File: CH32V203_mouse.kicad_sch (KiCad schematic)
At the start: 30 parts, among them J1 USB_C_Receptacle_USB2.0_16P_u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, J2 Conn_01x05_Pin, J3 Conn_01x04_Pin, SW1 SW_Push, U1 CH32V203G6U6, U2 USBLC6-2SC6, U3 XC6206P332MR, X1 16MHz

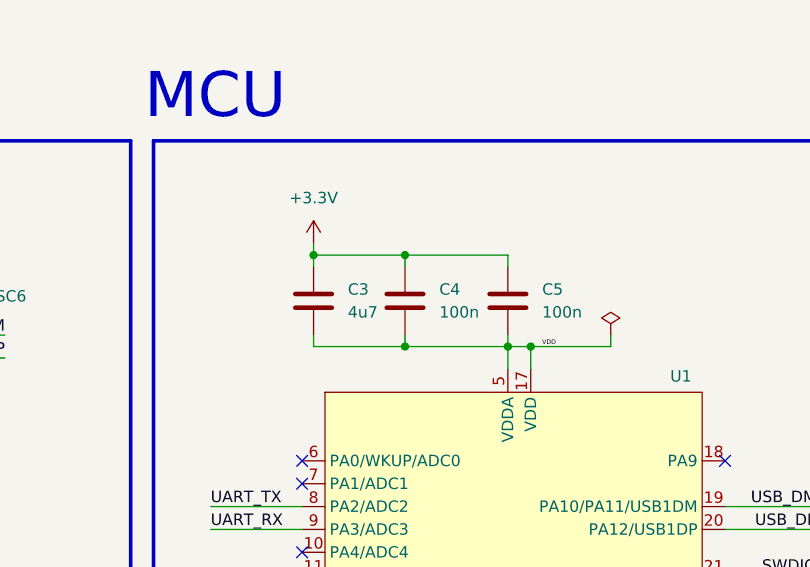
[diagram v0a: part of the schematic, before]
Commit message: Better PCB layout decoupling capacitors fixed changed LEDs footprints to correct ones
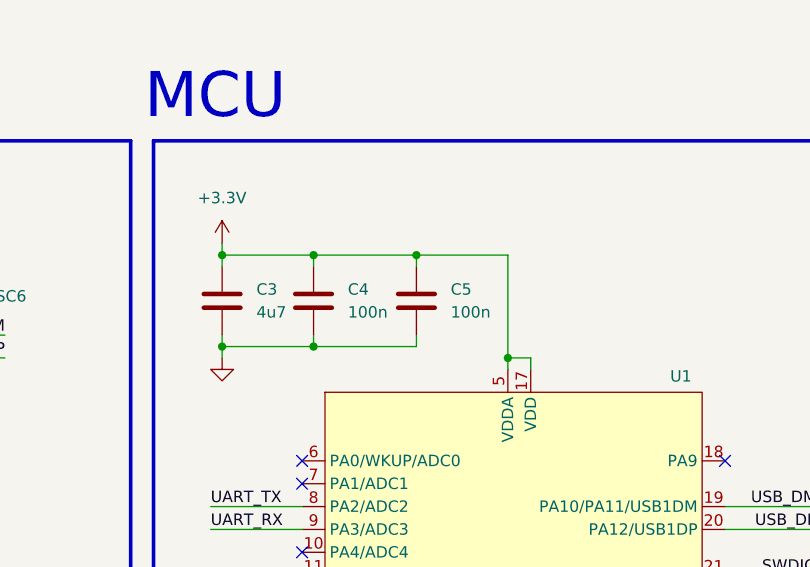
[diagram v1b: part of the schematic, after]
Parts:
- D1: footprint Capacitor_SMD:C_0402_1005Metric -> LED_SMD:LED_0603_1608Metric
- D2: footprint Capacitor_SMD:C_0402_1005Metric -> Diode_SMD:D_0603_1608Metric
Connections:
- net +3.3V: now also U1.17 (VDD), U1.5 (VDDA)
- net GND: now also C3.2, C4.2, C5.2
- removed net VDD: C3.2, C4.2, C5.2, U1.17 (VDD), U1.5 (VDDA)
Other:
- moved on the sheet: C3, C4, C5

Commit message: Changed stack up to a 4-layer board
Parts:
- D2: footprint Diode_SMD:D_0603_1608Metric -> LED_SMD:LED_0603_1608Metric
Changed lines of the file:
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@@
 			)
 		)
-		(property "Footprint" "Diode_SMD:D_0603_1608Metric"
+		(property "Footprint" "LED_SMD:LED_0603_1608Metric"
 			(at 259.08 52.07 0)
 			(effects

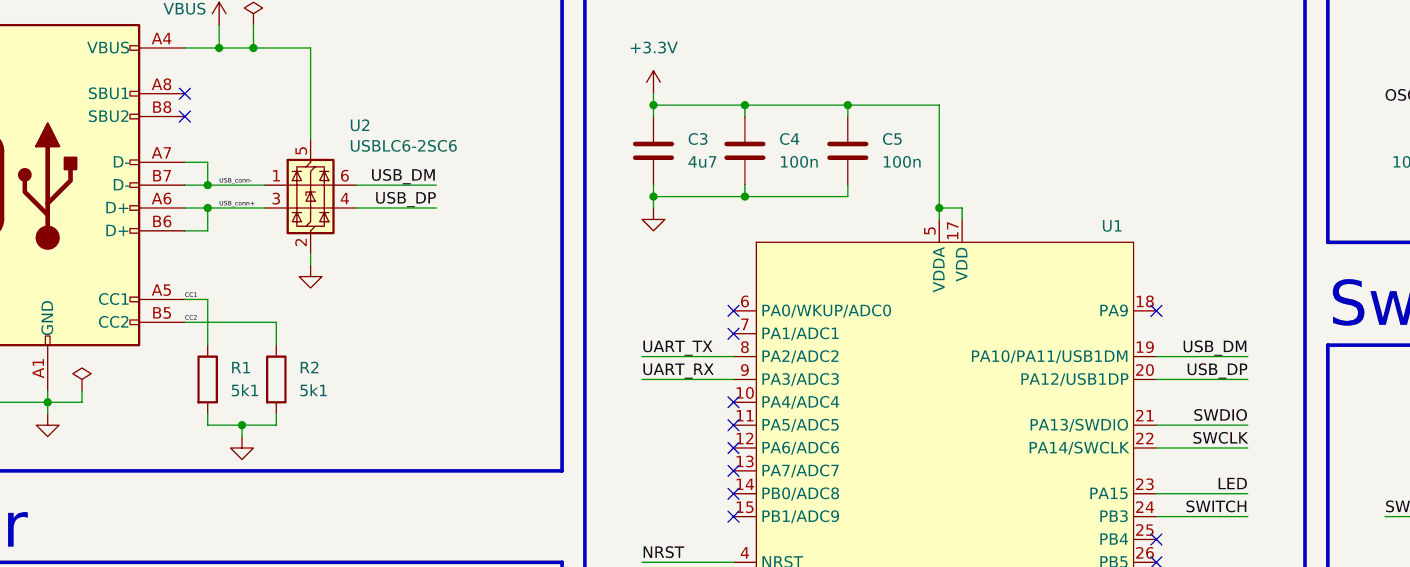
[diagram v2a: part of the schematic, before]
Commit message: Signals routed Constraints updated USB labels fixed
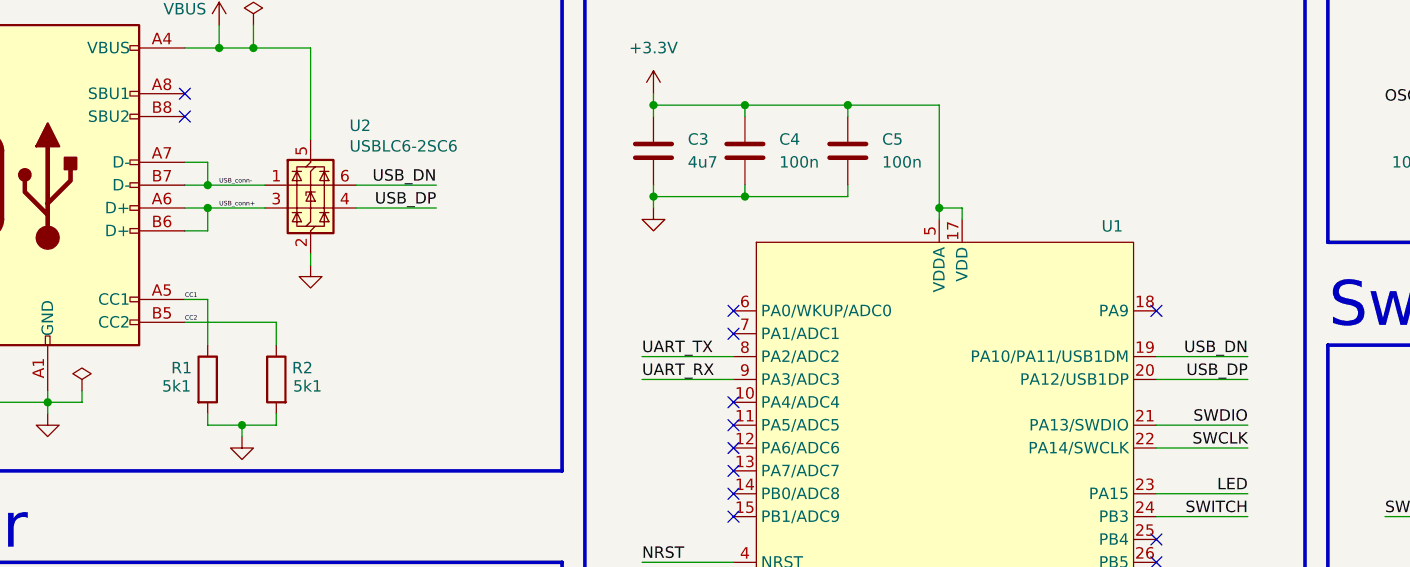
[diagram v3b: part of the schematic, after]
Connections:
- net USB_DM renamed USB_DN
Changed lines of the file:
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@@
 		)
 	)
-	(label "USB_DM"
+	(label "USB_DN"
 		(at 86.36 63.5 180)
 		(fields_autoplaced yes)
@@
 		)
 	)
-	(label "USB_DM"
+	(label "USB_DN"
 		(at 176.53 82.55 180)
 		(fields_autoplaced yes)
@@
 		(on_board yes)
 		(dnp no)
-		(fields_autoplaced yes)
 		(property "Reference" "R1"
-			(at 63.5 83.8199 0)
+			(at 56.896 83.82 0)
 			(effects
 				(font
@@
 		)
 		(property "Value" "5k1"
-			(at 63.5 86.3599 0)
+			(at 55.88 85.852 0)
 			(effects
 				(font
@@
 		(lib_id "Device:R")
 		(at 68.58 85.09 0)
-		(unit 1)
-		(exclude_from_sim no)
-		(in_bom yes)
-		(on_board yes)
-		(dnp no)
-		(fields_autoplaced yes)
+		(mirror y)
+		(unit 1)
+		(exclude_from_sim no)
+		(in_bom yes)
+		(on_board yes)
+		(dnp no)
 		(property "Reference" "R2"
-			(at 71.12 83.8199 0)
+			(at 72.644 83.82 0)
 			(effects
 				(font
@@
 		)
 		(property "Value" "5k1"
-			(at 71.12 86.3599 0)
+			(at 73.66 85.852 0)
 			(effects
 				(font
@@
 		)
 		(property "Footprint" "Resistor_SMD:R_0402_1005Metric"
-			(at 66.802 85.09 90)
-			(effects
-				(font
+			(at 70.358 85.09 90)
+			(effects
+				(font

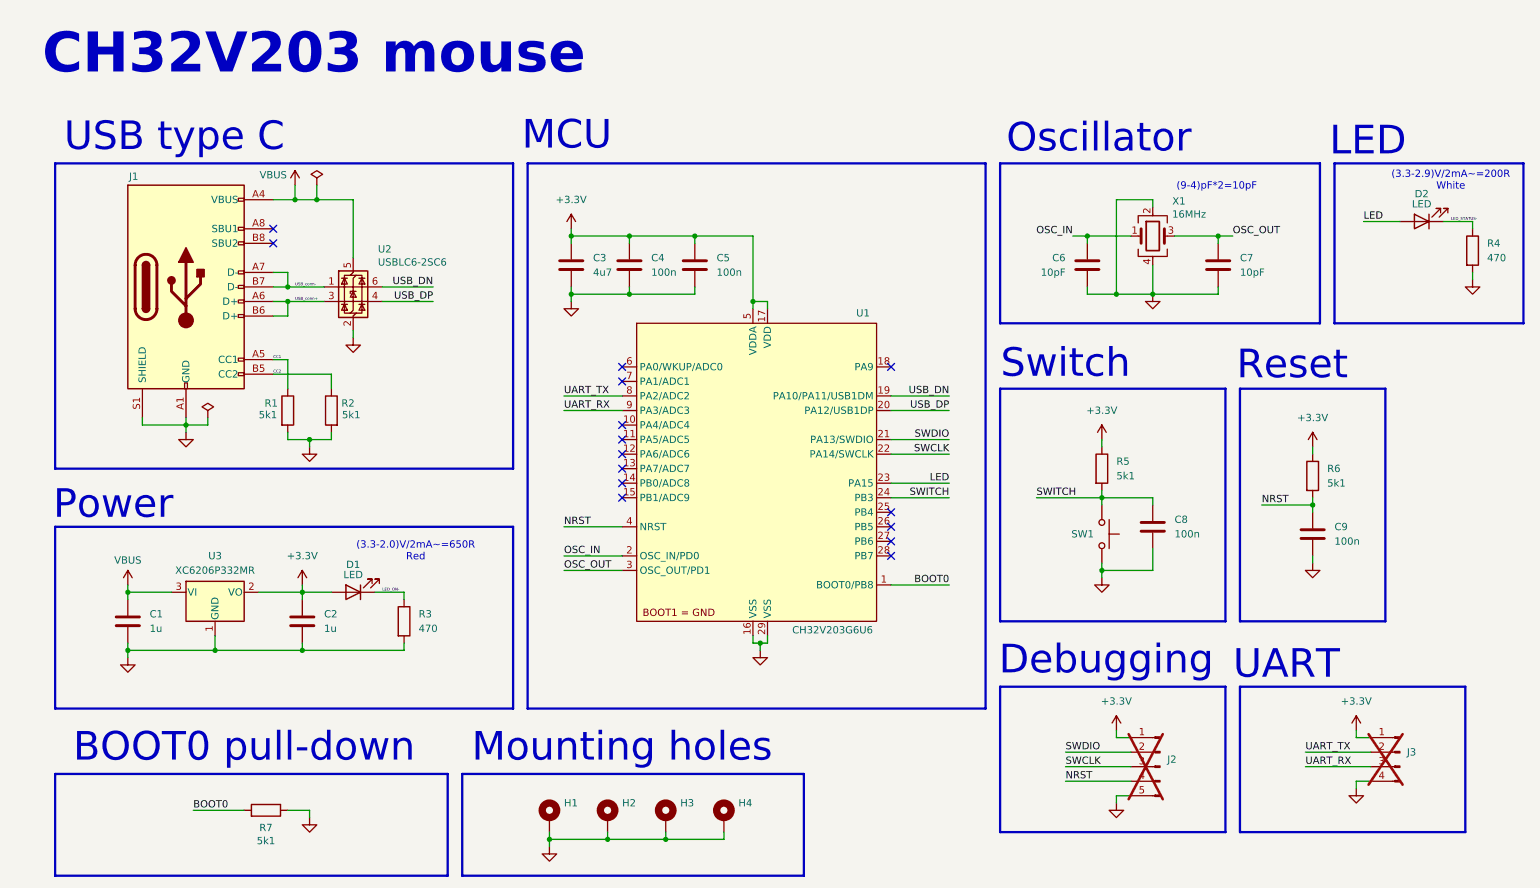
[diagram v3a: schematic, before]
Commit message: Final touches making sure fabrication files are compatible with JLCPCB
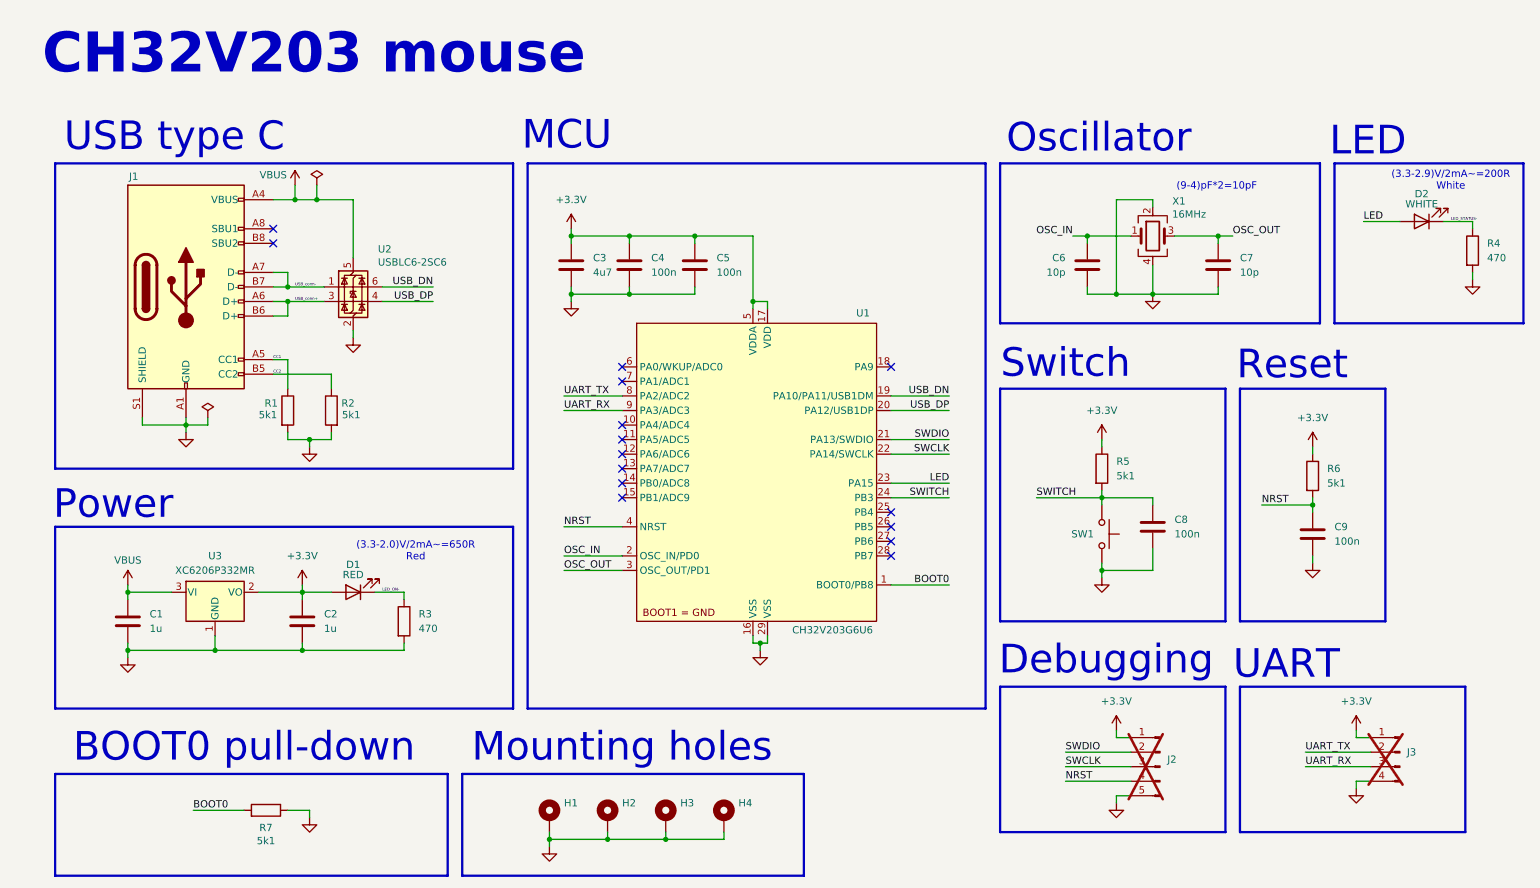
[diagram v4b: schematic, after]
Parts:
- C1, C2: JLCPCB Part # (none) -> C15849; JLCPCB site (none) -> https://jlcpcb.com/partdetail/16531-CL10A105KB8NNNC/C15849
- C3: JLCPCB Part # (none) -> C19666; JLCPCB site (none) -> https://jlcpcb.com/partdetail/20375-CL10A475KO8NNNC/C19666
- C4, C5, C8, C9: JLCPCB Part # (none) -> C1525; JLCPCB site (none) -> https://jlcpcb.com/partdetail/1877-CL05B104KO5NNNC/C1525
- C6, C7: value 10pF -> 10p; JLCPCB Part # (none) -> C32949; JLCPCB site (none) -> https://jlcpcb.com/partdetail/33914-CL05C100JB5NNNC/C32949
- D1: value LED -> RED; JLCPCB Part # (none) -> C2286; JLCPCB site (none) -> https://jlcpcb.com/partdetail/Hubei_KENTOElec-KT0603R/C2286
- D2: value LED -> WHITE; JLCPCB Part # (none) -> C2290; JLCPCB site (none) -> https://jlcpcb.com/partdetail/Hubei_KENTOElec-KT0603W/C2290
- J1: JLCPCB Part # (none) -> C2927038; JLCPCB site (none) -> https://jlcpcb.com/partdetail/DEALON-USB_TYPE_C018/C2927038
- J2, J3, SW1: now left out of the parts list
- R1, R2, R5, R6, R7: JLCPCB Part # (none) -> C25905; JLCPCB site (none) -> https://jlcpcb.com/partdetail/26648-0402WGF5101TCE/C25905
- R3, R4: JLCPCB Part # (none) -> C25117; JLCPCB site (none) -> https://jlcpcb.com/partdetail/25860-0402WGF4700TCE/C25117
- U1: JLCPCB Part # (none) -> C5142280; JLCPCB site (none) -> https://jlcpcb.com/partdetail/WCH_Jiangsu_Qin_Heng-CH32V203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
- U2: JLCPCB Part # (none) -> C5180279; JLCPCB site (none) -> https://jlcpcb.com/partdetail/ElecSuper-USBLC6_4SC6ES/C5180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
- U3: JLCPCB Part # (none) -> C5446; JLCPCB site (none) -> https://jlcpcb.com/partdetail/TorexSemicon-XC6206P332MRG/C5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
- X1: JLCPCB Part # (none) -> C13738; JLCPCB site (none) -> https://jlcpcb.com/partdetail/YXC_CrystalOscillators-X32251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

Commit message: Consolidated debugging and UART connectors and assigned them JST footprint reduced mounting holes' count to two and size to M2
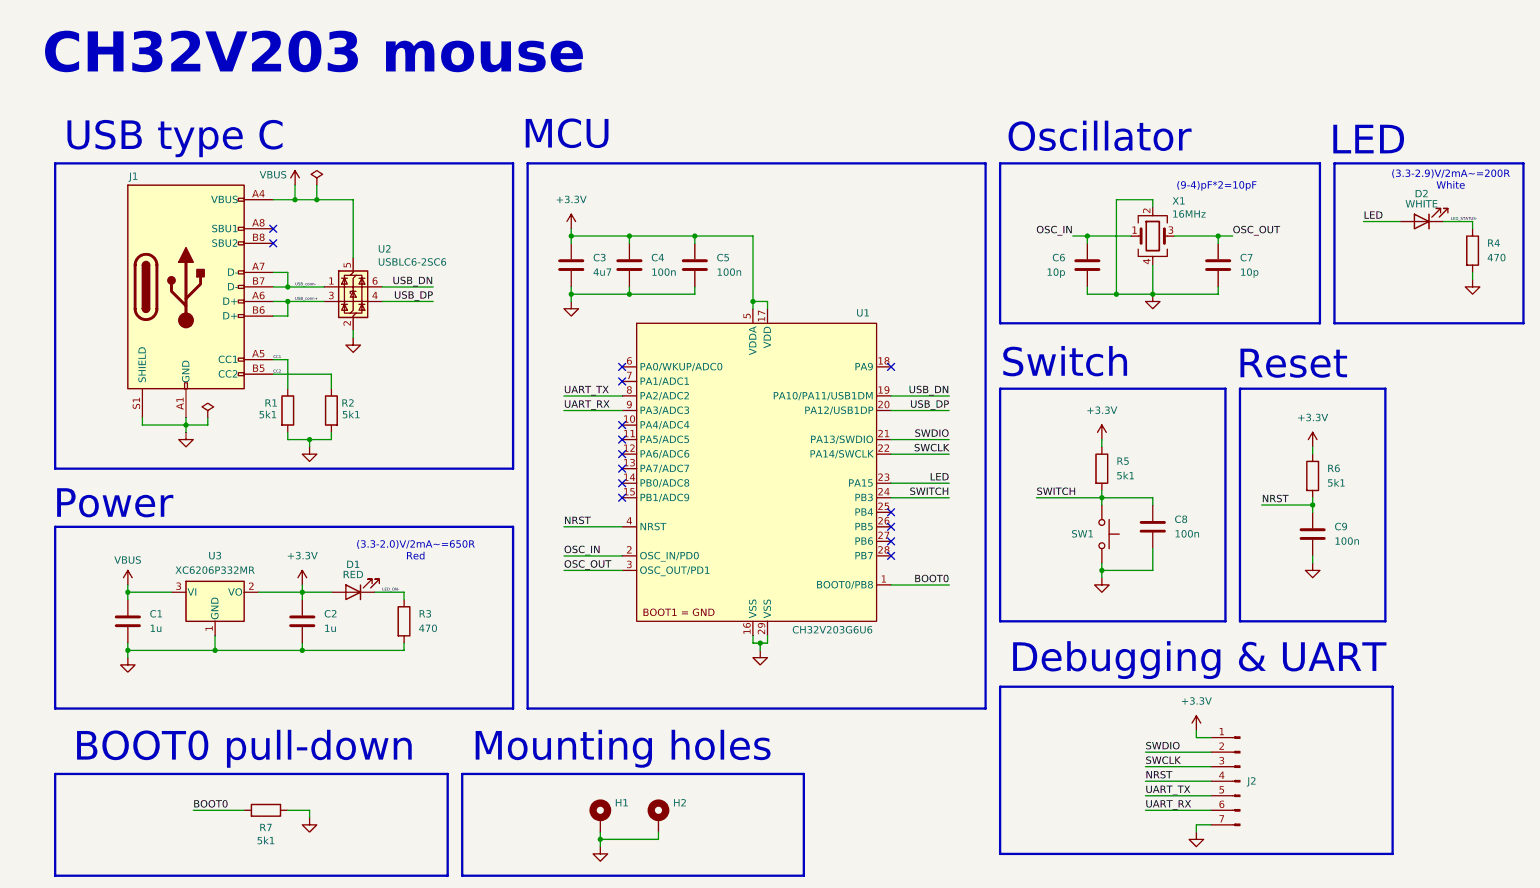
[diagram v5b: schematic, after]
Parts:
- removed H3, H4: MountingHole_Pad, MountingHole:MountingHole_3.2mm_M3_DIN965_Pad, symbol Mechanical:MountingHole_Pad
- removed J2: Conn_01x05_Pin, Connector_PinHeader_2.54mm:PinHeader_1x05_P2.54mm_Vertical, symbol Connector:Conn_01x05_Pin
- removed J3: Conn_01x04_Pin, Connector_PinHeader_2.54mm:PinHeader_1x04_P2.54mm_Vertical, symbol Connector:Conn_01x04_Pin
- added J2: Conn_01x07_Pin, Connector_JST:JST_XH_B7B-XH-A_1x07_P2.50mm_Vertical, symbol Connector:Conn_01x07_Pin
- H1, H2: footprint MountingHole:MountingHole_3.2mm_M3_DIN965_Pad -> MountingHole:MountingHole_2.2mm_M2_DIN965_Pad
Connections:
- net +3.3V: now also J2.1 (Pin_1)
- net GND: now also J2.7 (Pin_7)
- net NRST: now also J2.4 (Pin_4)
- net SWCLK: now also J2.3 (Pin_3)
- net SWDIO: now also J2.2 (Pin_2)
- net UART_RX: now also J2.6 (Pin_6)
- net UART_TX: now also J2.5 (Pin_5)
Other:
- note added: "Debugging & UART"
- note removed: "Debugging"
- note removed: "UART"
- moved on the sheet: H1, H2

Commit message: Decreased connector's size
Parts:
- J2: footprint Connector_JST:JST_XH_B7B-XH-A_1x07_P2.50mm_Vertical -> Connector_JST:JST_ZH_B7B-ZR_1x07_P1.50mm_Vertical
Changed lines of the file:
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@@
 			)
 		)
-		(property "Footprint" "Connector_JST:JST_XH_B7B-XH-A_1x07_P2.50mm_Vertical"
+		(property "Footprint" "Connector_JST:JST_ZH_B7B-ZR_1x07_P1.50mm_Vertical"
 			(at 227.33 149.86 0)
 			(effects

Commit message: PCB finished some parts excluded from BOM copper pours on top and bottom layers stitching vias
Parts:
- J1, J2: now left out of the parts list
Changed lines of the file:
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@@
 		(unit 1)
 		(exclude_from_sim no)
-		(in_bom yes)
+		(in_bom no)
 		(on_board yes)
 		(dnp no)
@@
 		(unit 1)
 		(exclude_from_sim no)
-		(in_bom yes)
-		(on_board yes)
-		(dnp no)
+		(in_bom no)
+		(on_board yes)
+		(dnp no)
